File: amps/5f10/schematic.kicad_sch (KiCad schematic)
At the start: 42 parts, among them T1 PP OT

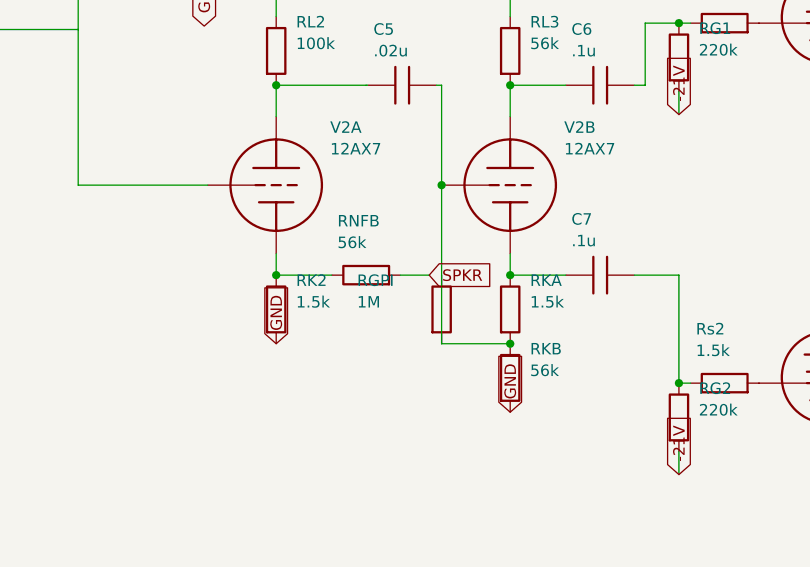
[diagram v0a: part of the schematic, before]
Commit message: Fix: schematic sheet polish — bias-supply and label crowding
- 5F4 + JTM45: lift bias-supply branch clear of the A4 title-block corner
- 5F2-A + 5F10: relieve tone-pot / cathodyne label crowding
- Regenerated schematics via draw_*.py; public/ mirrors synced by build

🤖 Generated with [Claude Code](https://claude.com/claude-code)

Co-Authored-By: Claude Opus 4.8 (1M context) <noreply@anthropic.com>
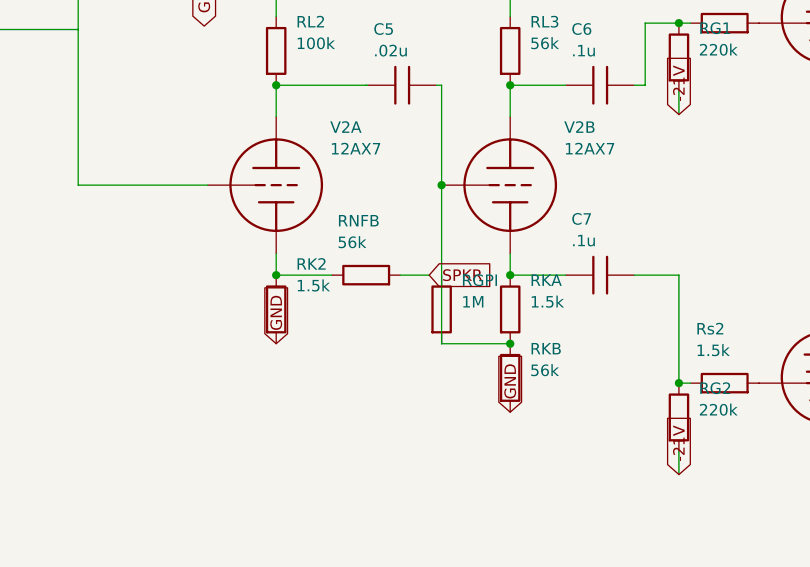
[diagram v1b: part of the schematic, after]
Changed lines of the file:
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@@
   (symbol (lib_id "cx:R") (at 114 123.81 0) (unit 1)
     (in_bom yes) (on_board yes)
-    (property "Reference" "RK2" (at 116.2 120.61 0) (effects (font (size 1.27 1.27)) (justify left)))
-    (property "Value" "1.5k" (at 116.2 123.01 0) (effects (font (size 1.27 1.27)) (justify left))))
+    (property "Reference" "RK2" (at 116.2 118.81 0) (effects (font (size 1.27 1.27)) (justify left)))
+    (property "Value" "1.5k" (at 116.2 121.21 0) (effects (font (size 1.27 1.27)) (justify left))))
   (global_label "GND" (shape input) (at 114 127.62 270)
     (effects (font (size 1.27 1.27)) (justify left)))
@@
   (symbol (lib_id "cx:R") (at 132.38 123.81 0) (unit 1)
     (in_bom yes) (on_board yes)
-    (property "Reference" "RGPI" (at 122.98 120.61 0) (effects (font (size 1.27 1.27)) (justify left)))
-    (property "Value" "1M" (at 122.98 123.01 0) (effects (font (size 1.27 1.27)) (justify left))))
+    (property "Reference" "RGPI" (at 134.58 120.61 0) (effects (font (size 1.27 1.27)) (justify left)))
+    (property "Value" "1M" (at 134.58 123.01 0) (effects (font (size 1.27 1.27)) (justify left))))
   (wire (pts (xy 132.38 127.62) (xy 140 127.62))
     (stroke (width 0) (type default)))

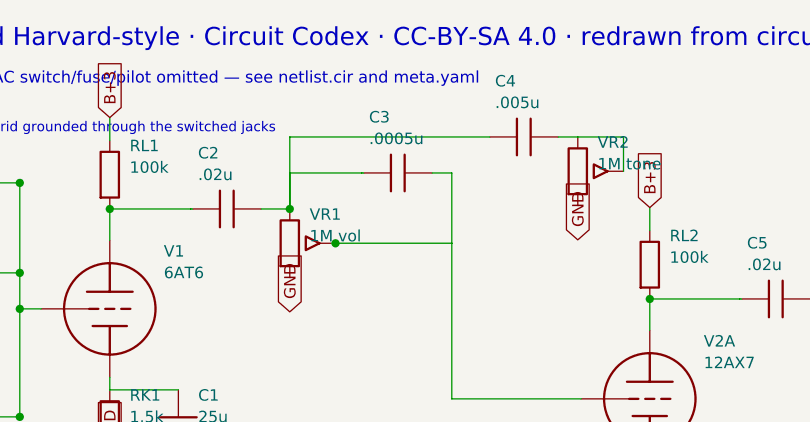
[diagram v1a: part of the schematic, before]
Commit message: Fix: one lettering convention per surface, engine-enforced; legend inside the viewBox
WS3 — layout pipeline + cross-surface value-consistency engine.

## One convention per surface (docs/lettering-conventions.md, new)

The same part stated its value in several notations at once. 5E3 C6 and 5D3 C6
rendered "5n" on the schematic, "0.005 µF · 600 V" in the parts list and
"0.005 µF" on the board. 5F6-A RD1 printed "4,700 Ω" beside neighbours printing
"15 kΩ". check_value_consistency proves the surfaces name the same QUANTITY; it
cannot see that they name it three ways. So each surface now has exactly one
convention and every one of them is gated:

* house units in bom.yaml/prose — engineering prefix with the mantissa 1…999,
  pF below 1000 pF and µF at and above it, no comma-grouped thousands. 19 values
  normalised (5E6-A, 5F6-A, 5F10, 6161, 6G2, 6G5, 6G6-B).
* schematic drafting shorthand — the unit letter is the SI prefix of the house
  unit, in the amp's declared idiom (meta.yaml conventions.notation: us|uk).
  British RKM/nanofarad practice on the Hiwatt and the 2204 is DECLARED, not
  normalised away; it is what those source drawings letter. Secondary ratings
  are space-separated fields with their own unit ("20u 600V"), never the era's
  dashed shorthand and never the house middot. 30 symbol values corrected across
  ten draw scripts.
* era sheet lettering — generated only, by era_pair(); documented cases and a
  corpus round-trip sweep in test_era_values.py, now 57 cases.

## Era-lettering fall-throughs closed

A value era_pair() refuses came back as the house string, and a house string can
be a whole sentence. Fixed at the source rather than per case:

* body_value() — a parenthetical GLOSS is never lettered on a component body.
  "selenium (silicon diode in modern builds)" was lettered in full on the 5E4-A
  and ran off the left edge of the page.
* twin cans letter as the era sheets did: 25 µF + 25 µF -> "25/25MFD".
* a repeat count is not a rating: "(×2)" com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
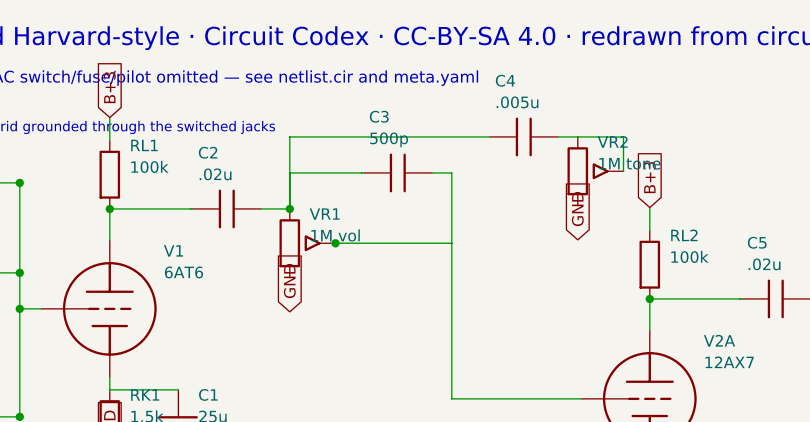
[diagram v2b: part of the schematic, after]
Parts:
- C3: value .0005u -> 500p
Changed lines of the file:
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@@
     (in_bom yes) (on_board yes)
     (property "Reference" "C3" (at 82.8 78.7 270) (effects (font (size 1.27 1.27)) (justify left)))
-    (property "Value" ".0005u" (at 82.8 81.1 270) (effects (font (size 1.27 1.27)) (justify left))))
+    (property "Value" "500p" (at 82.8 81.1 270) (effects (font (size 1.27 1.27)) (justify left))))
   (wire (pts (xy 82 84.9) (xy 82.19 84.9))
     (stroke (width 0) (type default)))

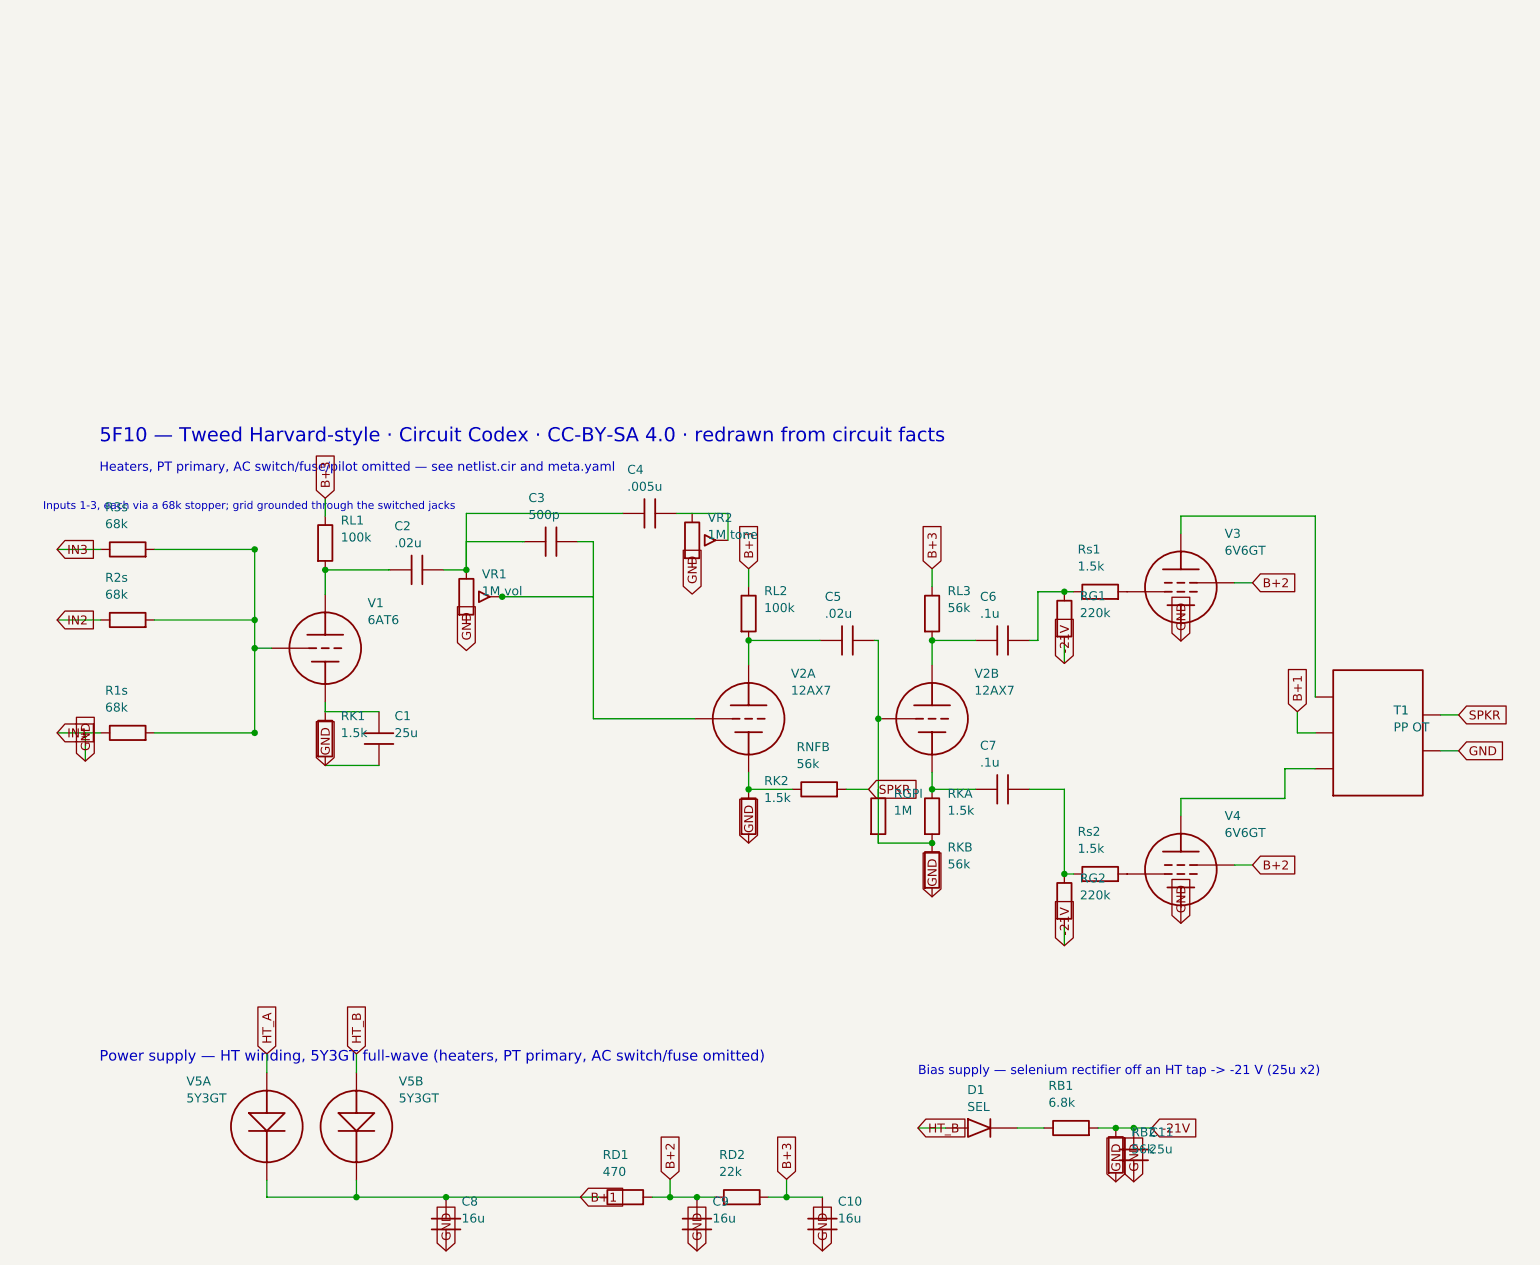
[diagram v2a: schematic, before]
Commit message: Update: regenerate every drawing the four merged units changed
The four parallel units all rewrote generators, so their committed artifacts
were each generated against only their own third of the merged pipeline. Every
schematic, both layout styles, the social cards and the manifest are rebuilt
here from the merged sources, so what ships is what the merged generators draw.

One integration fault the rebuild exposed, invisible to any single unit:

- 5E5-A: the note explaining that the Presence wiper and the 100k feedback
  resistor land on V3A's GRID (not its cathode, as on the 5F4) was added as a
  hand-placed `s.text()` at a coordinate chosen before the sheet gained a
  reserved notes band. Merged, it printed through the -32V bias label. Moved to
  `note()`, which wraps prose into that band — the exact failure mode the band
  was built to end.

Three conflicts resolved against docs/lettering-conventions.md rather than by
picking a side, since two units had corrected the same lines for different
reasons:

- 5E5-A tone/feedback caps take the corrected designators (C7, C8, C9, RNF —
  `C_tr1`/`C_NFB` were generator identifiers that had leaked onto a published
  board) with the house-derived lettering (`.01u 400V`, `500p`, `.1u 200V`).
  Dropping the working voltage or writing `.0005u` would have lost a rating the
  source prints and re-broken the pF/µF decade rule.
- 5D3 C6 and 6G6-B's three cathode resistors take the SI-prefix form the
  convention binds (`.005u`, `2.7k`, `1.5k`), keeping the ground-flag direction
  fix and the removal of the second `gnd()` that shorted each cathode it biased.
- 5F6-A's bias supply keeps both 8 µF cans drawn — the second was previously a
  parenthetical claiming one of two was shown — at the coordinates that clear
  the title-block strip.

All gates green, including check_value_consistency at zero disagreements.

🤖 Generated with [Claude Code](https://claude.com/claude-code)

Co-Authored-By: Claude Fable 5 <noreply@anthropic.com>
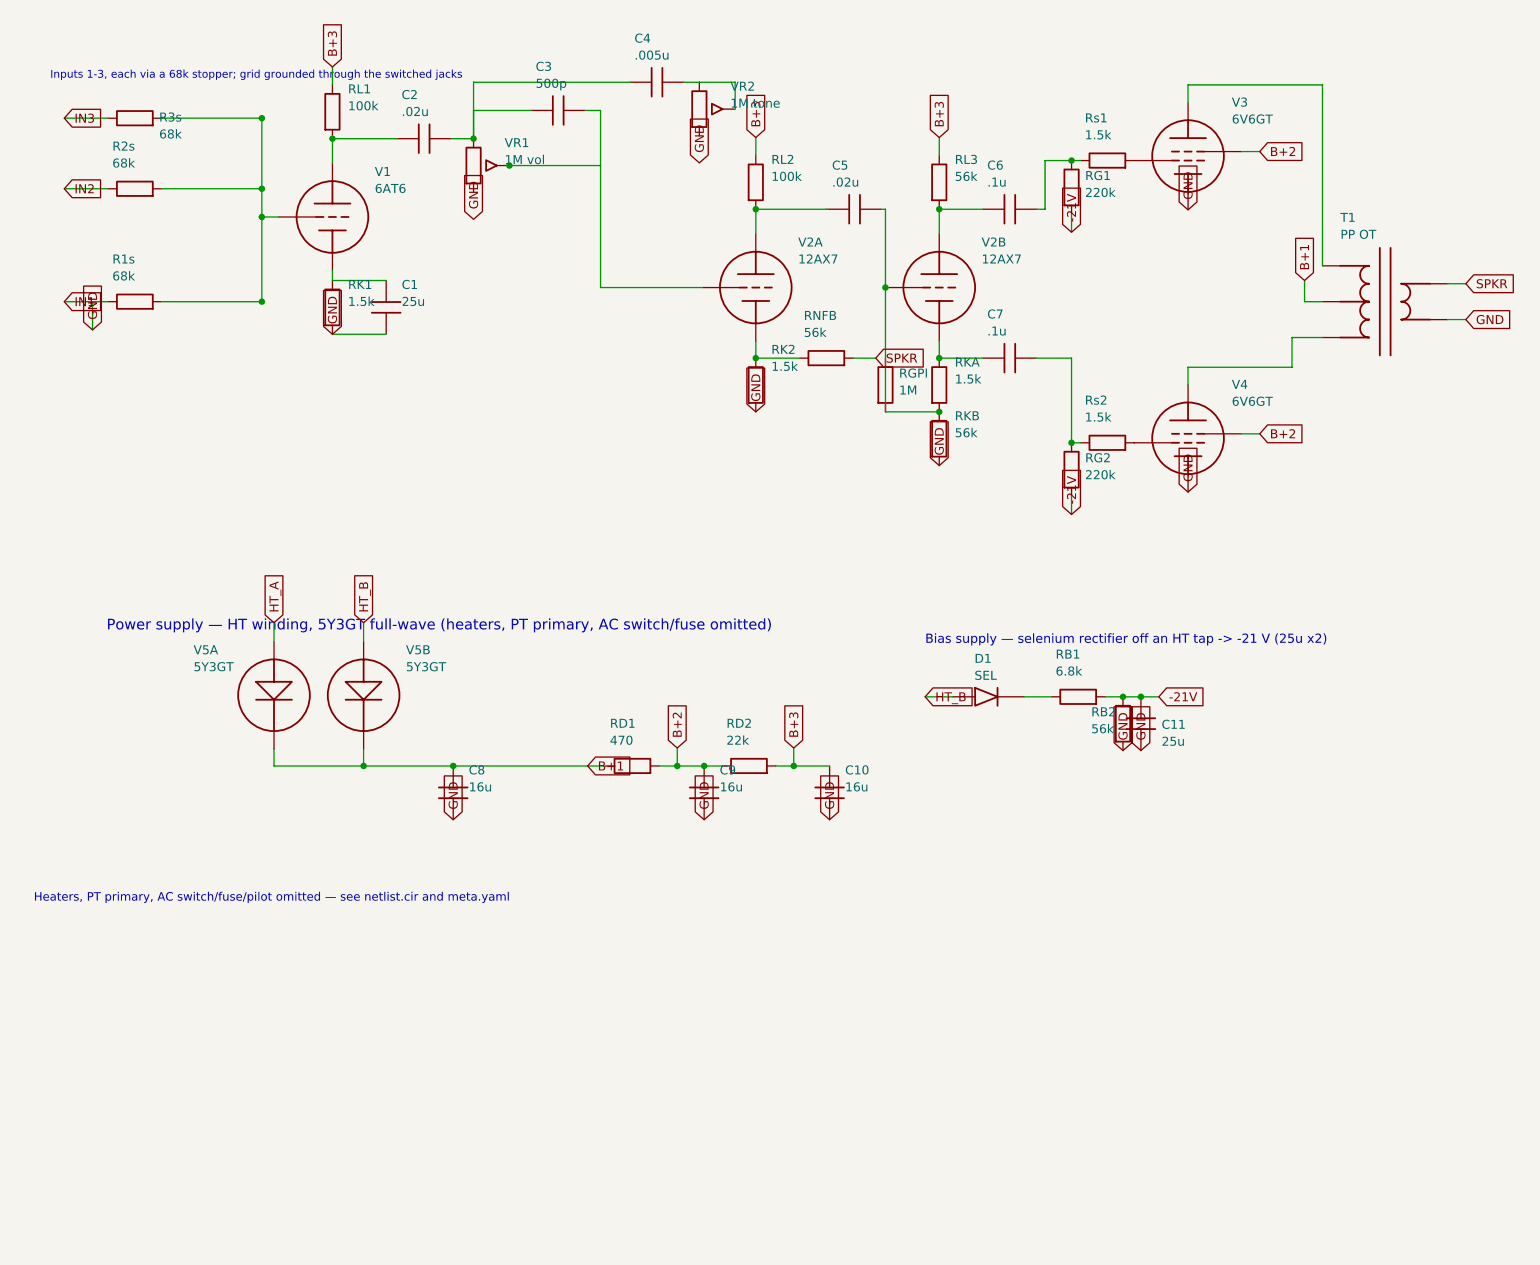
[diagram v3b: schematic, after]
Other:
- note removed: "5F10 — Tweed Harvard-style · Circuit Codex · CC-BY-SA 4.0 · redrawn from circuit facts"
- company: (none) -> Circuit Codex
- title: (none) -> 5F10 — Tweed Harvard-style
